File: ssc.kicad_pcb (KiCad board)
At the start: 4 copper layers, 98.8 x 85.1 mm, 25 parts, among them J1 IRQ ENABLE, J2 RS-232 OUT, P1 A2Bus, U1 74HCT245, U2 28C256, U3 1.8432M, U4 SSCGLU, U5 W65C51NxP, U6 MAX3232, U7 MAX3232

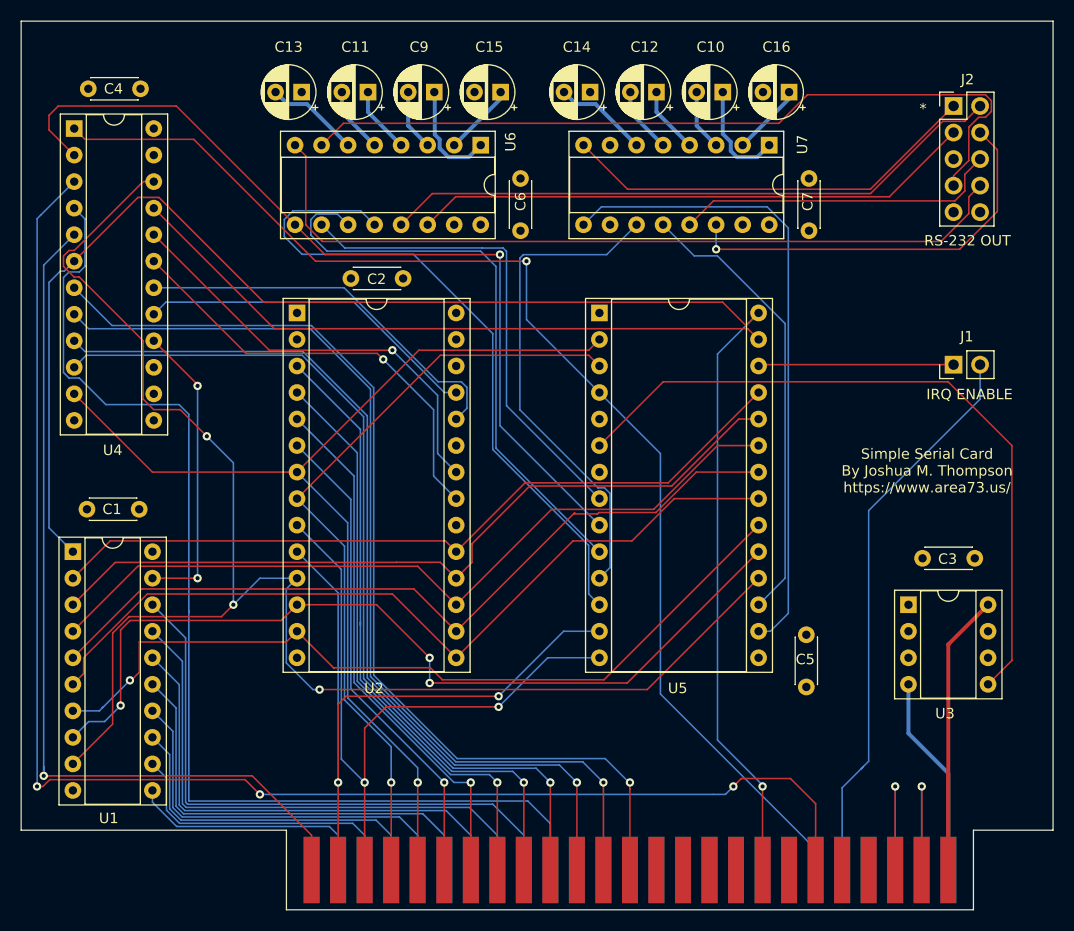
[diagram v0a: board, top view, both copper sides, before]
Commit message: Changed to two layer board
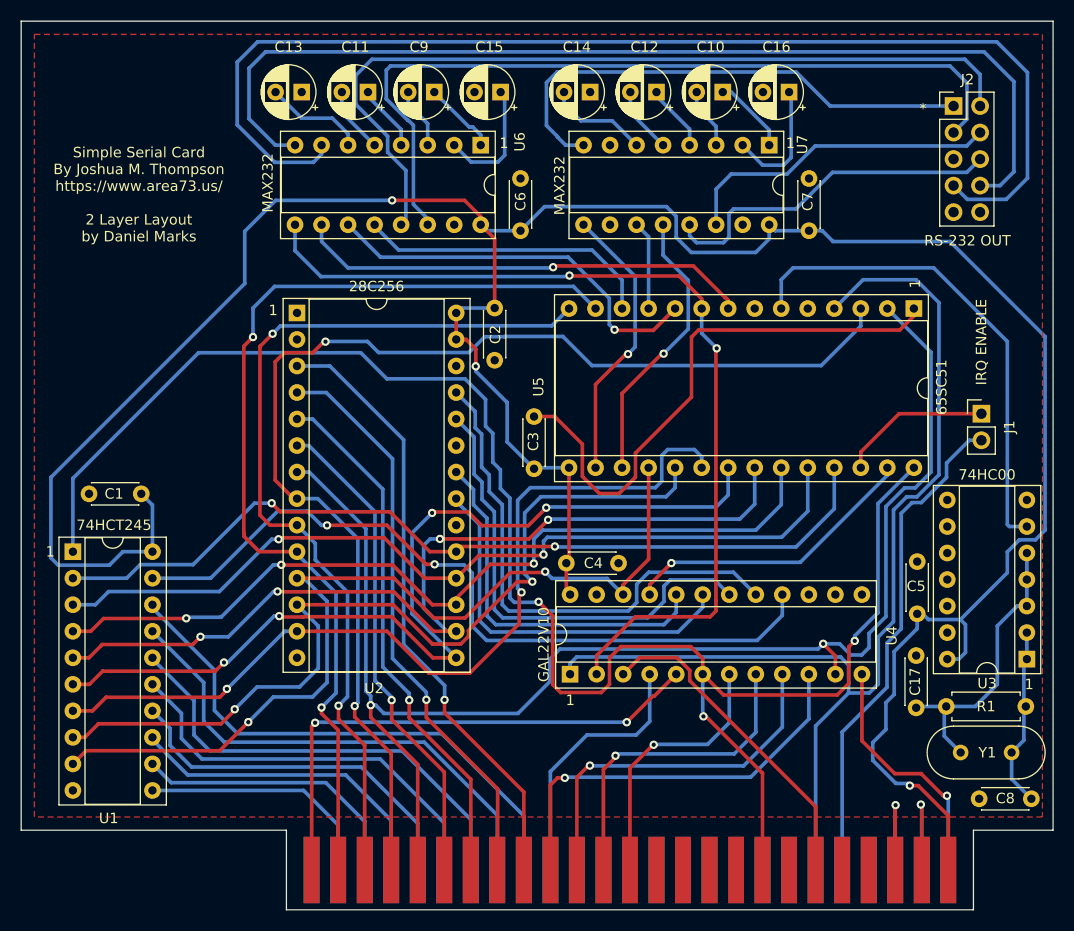
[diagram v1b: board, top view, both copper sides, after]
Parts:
- added C17: 20 pF, Capacitor_THT:C_Disc_D4.3mm_W1.9mm_P5.00mm, F.Cu at (187.3, 107.7)
- added C8: 20 pF, Capacitor_THT:C_Disc_D4.3mm_W1.9mm_P5.00mm, F.Cu at (198.3, 116.4)
- added R1: 1M, Resistor_THT:R_Axial_DIN0207_L6.3mm_D2.5mm_P7.62mm_Horizontal, F.Cu at (197.8, 107.5)
- added Y1: 1.8432 MHz, Crystal:Crystal_HC49-U_Vertical, F.Cu at (196.4, 111.9)
- U3: value 1.8432M -> 74HC00; footprint Package_DIP:DIP-8_W7.62mm_Socket -> Package_DIP:DIP-14_W7.62mm_Socket
- moved U4 70.6 mm to (154.2, 104.4), turned to 90 degrees
- moved C4 61.0 mm to (153.8, 93.8), turned to 0 degrees
- moved C3 43.1 mm to (150.7, 84.8), turned to 90 degrees
- moved U5 30.1 mm to (187.1, 69.4), turned to -90 degrees
- moved C5 12.7 mm to (187.4, 98.7)
- moved U3 12.5 mm to (197.9, 103.0), turned to 180 degrees
- moved C2 9.21 mm to (146.9, 69.4), turned to -90 degrees
- moved J1 5.40 mm to (193.5, 79.5), turned to 0 degrees
- moved C1 1.49 mm to (113.1, 87.2)
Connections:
- net R~W renamed R~{W}
- net ~DEVSEL renamed ~{DEVSEL}
- net ~IOSEL renamed ~{IOSEL}
- net ~IOSTRB renamed ~{IOSTRB}
- net ~IRQ renamed ~{IRQ}
- net ~LATCHCE renamed ~{LATCHCE}
- net ~RES renamed ~{RES}
- net ~ROMOE renamed ~{ROMOE}
- J2 pad 9: (no net) -> unconnected-(J2-Pad9)
- P1 pad 14: (no net) -> unconnected-(P1-Pad14)
- P1 pad 15: (no net) -> unconnected-(P1-Pad15)
- P1 pad 16: (no net) -> unconnected-(P1-Pad16)
- P1 pad 17: (no net) -> unconnected-(P1-Pad17)
- P1 pad 19: (no net) -> unconnected-(P1-Pad19)
- P1 pad 21: (no net) -> unconnected-(P1-Pad21)
- P1 pad 22: (no net) -> unconnected-(P1-Pad22)
- P1 pad 29: (no net) -> unconnected-(P1-Pad29)
- P1 pad 32: (no net) -> unconnected-(P1-Pad32)
- P1 pad 33: (no net) -> unconnected-(P1-Pad33)
- P1 pad 34: (no net) -> unconnected-(P1-Pad34)
- P1 pad 35: (no net) -> unconnected-(P1-Pad35)
- P1 pad 36: (no net) -> unconnected-(P1-Pad36)
- P1 pad 37: (no net) -> unconnected-(P1-Pad37)
- P1 pad 38: (no net) -> unconnected-(P1-Pad38)
- P1 pad 39: (no net) -> unconnected-(P1-Pad39)
- P1 pad 40: (no net) -> unconnected-(P1-Pad40)
- P1 pad 50: (no net) -> unconnected-(P1-Pad50)
- U3 pad 1: (no net) -> Net-(R1-Pad1)
- U3 pad 2: (no net) -> Net-(R1-Pad1)
- U3 pad 3: (no net) -> Net-(R1-Pad2)
- U3 pad 4: GND -> Net-(R1-Pad2)
- U3 pad 5: SERCLK -> Net-(R1-Pad2)
- U3 pad 6: (no net) -> SERCLK
- U3 pad 7: (no net) -> GND
- U3 pad 8: +5V -> unconnected-(U3-Pad8)
- U5 pad 5: (no net) -> unconnected-(U5-Pad5)
- U5 pad 7: (no net) -> unconnected-(U5-Pad7)
- U7 pad 7: (no net) -> unconnected-(U7-Pad7)
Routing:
- net +5V: track 27.0 -> 263.6 mm, vias 0 -> 3
- net ~{IOSTRB}: track 142.8 -> 31.6 mm, vias 3 -> 0
- net ~{DEVSEL}: track 108.4 -> 25.4 mm
- net A11: track 97.3 -> 25.7 mm
- net A10: track 93.7 -> 31.3 mm
- net D0: track 146.7 -> 87.8 mm, vias 3 -> 2
- net GND: track 19.4 -> 77.6 mm, vias 0 -> 1
- net A9: track 88.7 -> 35.6 mm
- net A8: track 86.1 -> 39.8 mm
- net ~{LATCHCE}: track 28.8 -> 74.1 mm
- net A2: track 74.4 -> 117.2 mm, vias 1 -> 2
- net Net-(U5-Pad11): track 47.5 -> 8.50 mm
- net Net-(J2-Pad7): track 76.4 -> 113.0 mm
- net Net-(U5-Pad12): track 65.2 -> 28.7 mm
- net A3: track 101.5 -> 137.0 mm, vias 1 -> 2
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- added copper zone on F.Cu, net GND
- removed copper zone on In1.Cu, net +5V
- removed copper zone on In2.Cu, net GND
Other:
- copper layers 4 -> 2
- net class Default removed
- net class Power removed
- board text added: "1"
- board text added: "28C256"
- board text added: "65SC51"
- board text added: "74HC00"
- board text added: "74HCT245"
- board text added: "GAL22V10"
- board text added: "MAX232"
- board text added: "Simple Serial Card By Joshua M. Thompson https://www.area73.us/ 2 Layer Layout by Daniel Marks"
- board text removed: "Simple Serial Card By Joshua M. Thompson https://www.area73.us/"

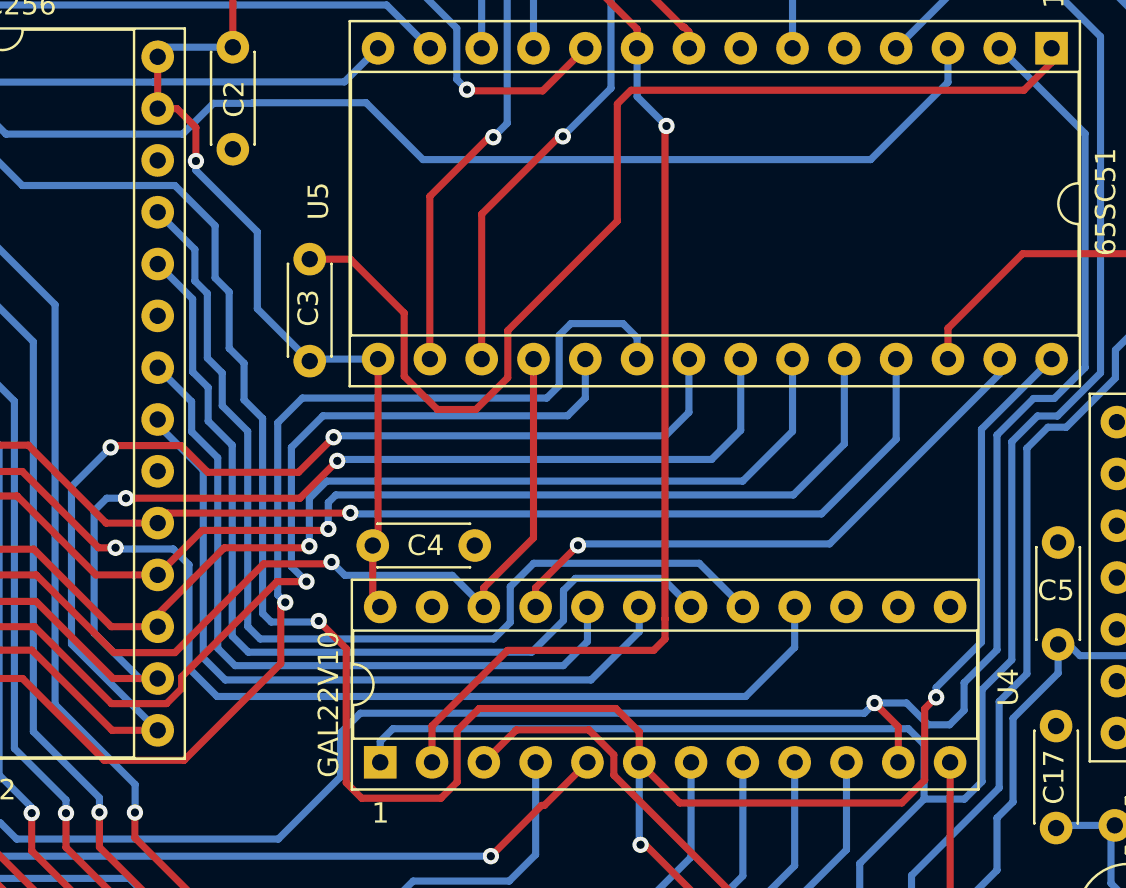
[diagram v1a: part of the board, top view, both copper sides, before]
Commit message: Fixed long ground path
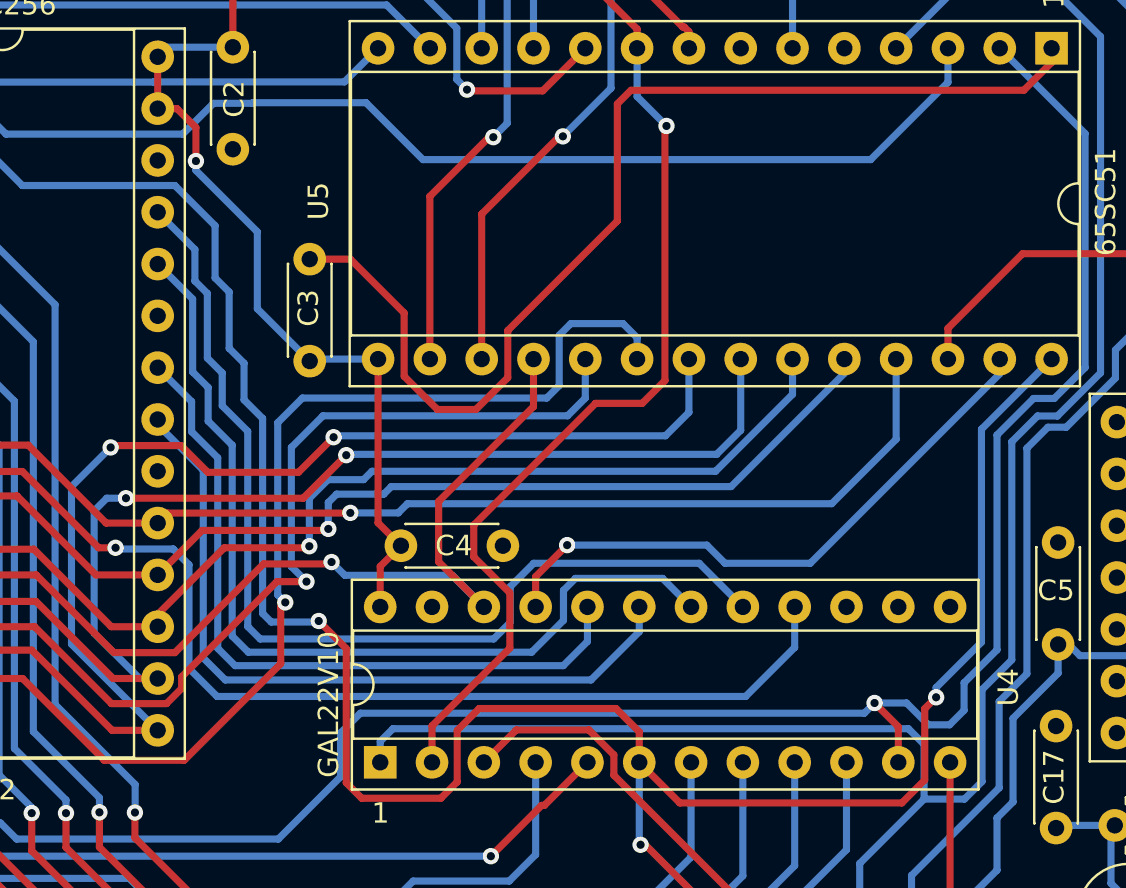
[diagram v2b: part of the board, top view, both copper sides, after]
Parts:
- moved C4 1.38 mm to (155.2, 93.8)
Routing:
- net D6: track 82.2 -> 80.2 mm
- net D0: track 87.8 -> 89.7 mm
- net Net-(U4-Pad2): track 88.9 -> 87.5 mm
- net D5: track 81.3 -> 80.2 mm
- net PHI2: track 28.8 -> 29.8 mm
- net +5V: track 263.6 -> 264.2 mm

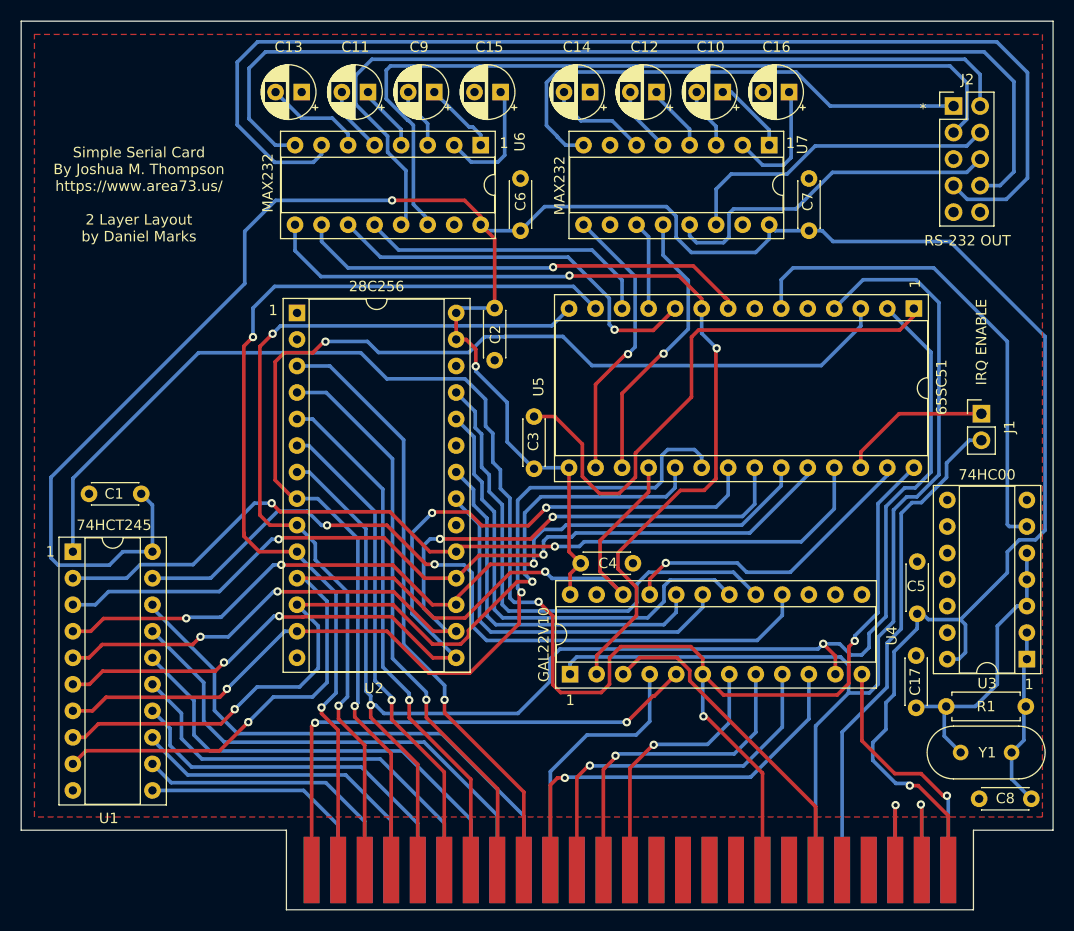
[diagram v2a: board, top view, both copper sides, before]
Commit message: Added NAND gate and labels
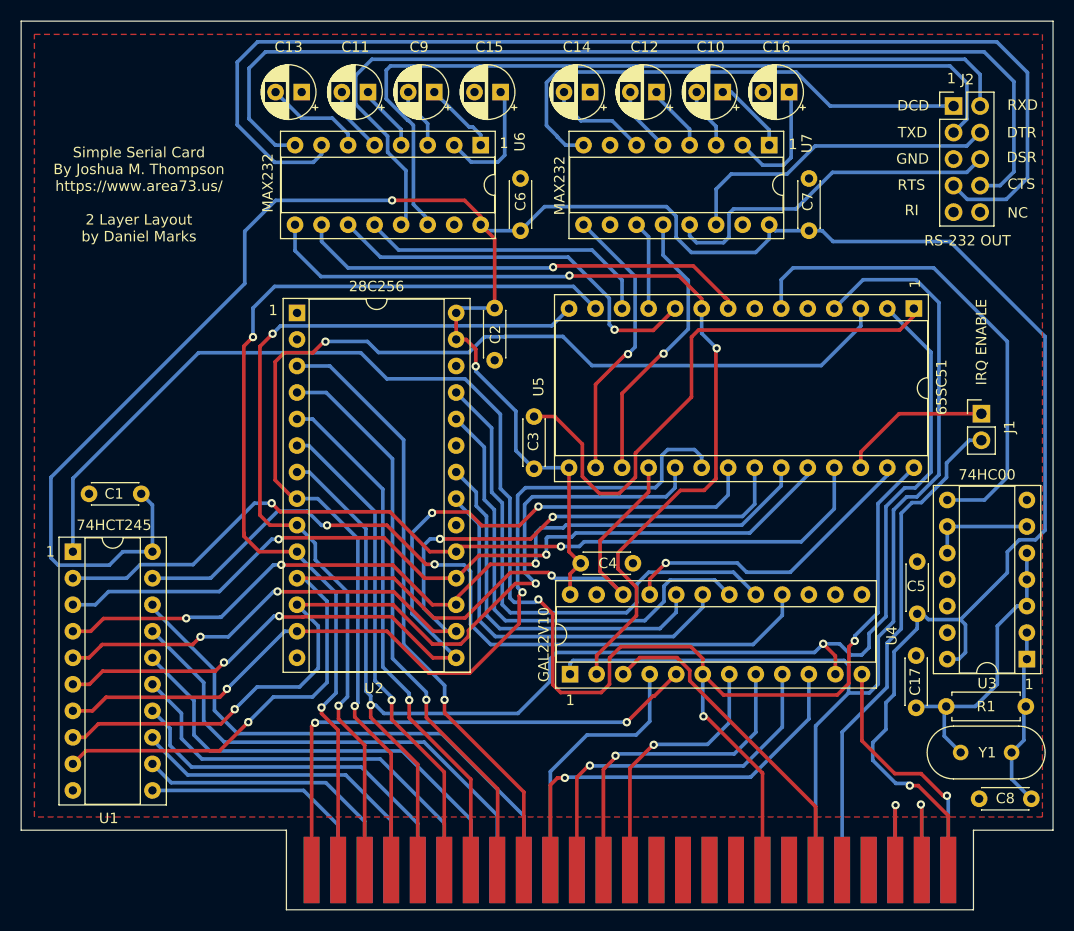
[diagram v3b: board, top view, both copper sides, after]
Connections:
- U3 pad 10: GND -> Net-(U3-Pad6)
- U3 pad 6: SERCLK -> Net-(U3-Pad6)
- U3 pad 8: unconnected-(U3-Pad8) -> SERCLK
- U3 pad 9: GND -> Net-(U3-Pad6)
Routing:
- net Net-(U3-Pad6): track 0.00 -> 10.2 mm
- net D1: track 84.3 -> 85.4 mm
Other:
- board text added: "CTS"
- board text added: "DCD"
- board text added: "DSR"
- board text added: "DTR"
- board text added: "GND"
- board text added: "NC"
- board text added: "RI"
- board text added: "RTS"
- board text added: "RXD"
- board text added: "TXD"
- board text removed: "*"
